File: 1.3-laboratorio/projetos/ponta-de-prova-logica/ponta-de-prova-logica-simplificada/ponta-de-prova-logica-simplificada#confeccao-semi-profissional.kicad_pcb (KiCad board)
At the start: 2 copper layers, 66 x 49.5 mm, 21 parts, among them J1 Conn_01x02, J2 PONTA DE PROVA, SW1 SW_DPDT_x2, U1 LM339

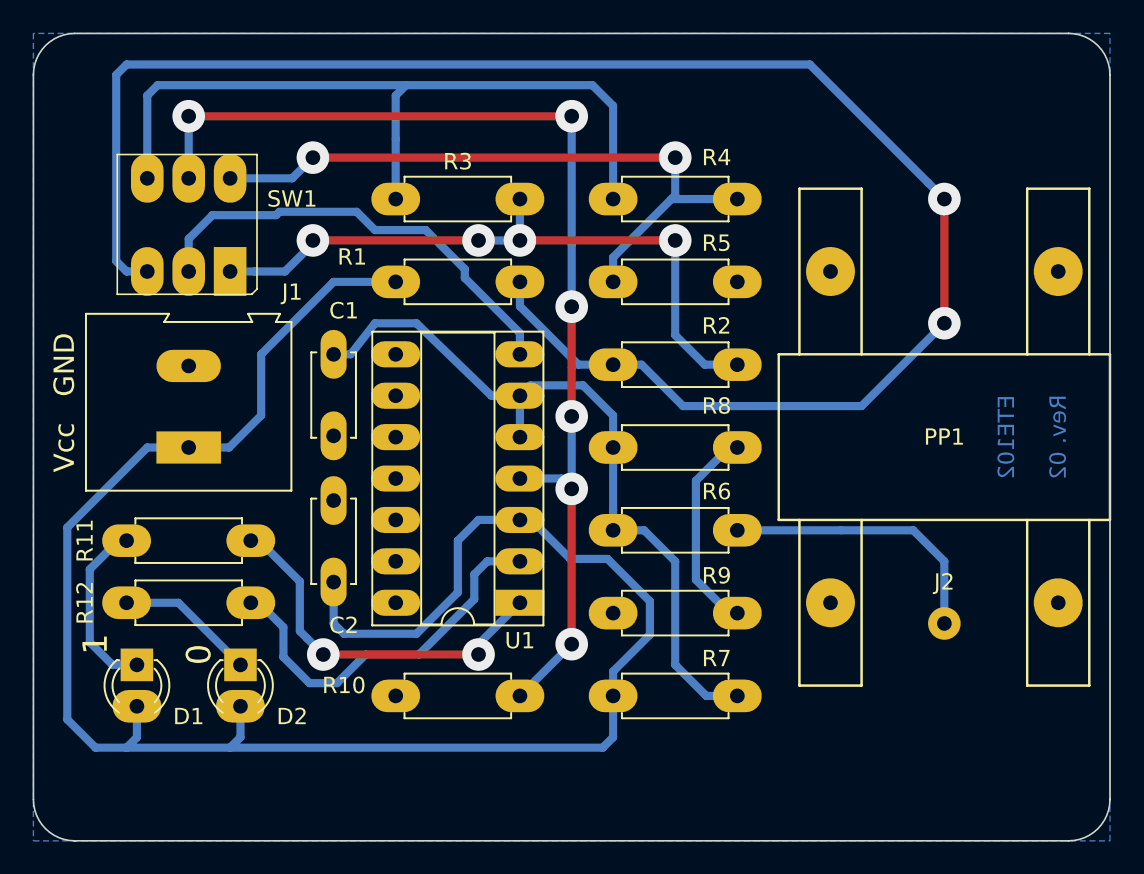
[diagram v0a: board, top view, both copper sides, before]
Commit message: Revisões no leiaute. Pontos de furação acrescentados, tamanho da placa e reposicionamento de algumas ilhas e trilhas.
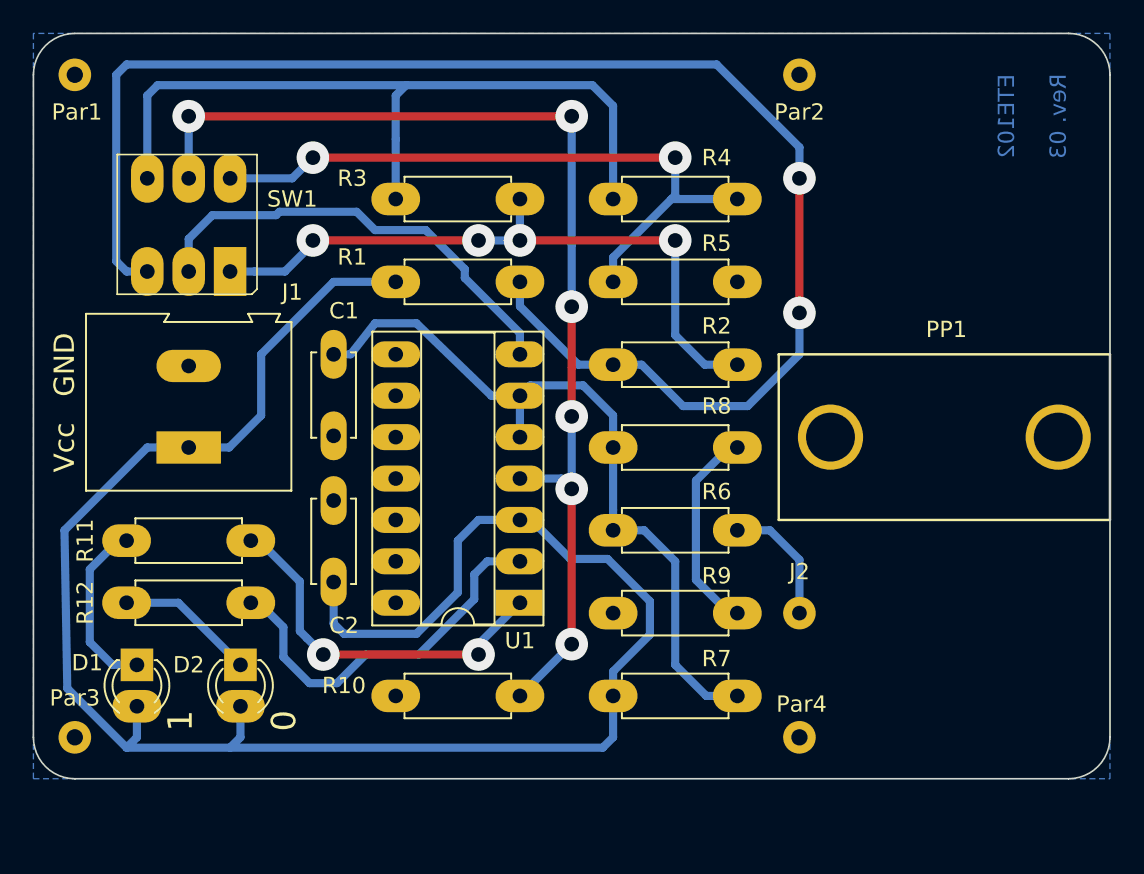
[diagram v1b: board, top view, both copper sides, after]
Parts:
- added Par1: MountingHole_1mm_M1_DIN965_Pad, MountingHole:MountingHole_2.2mm_M2_DIN965_Pad, F.Cu at (20.3, 21.0)
- added Par2: MountingHole_1mm_M1_DIN965_Pad, MountingHole:MountingHole_2.2mm_M2_DIN965_Pad, F.Cu at (64.8, 21.0)
- added Par3: MountingHole_1mm_M1_DIN965_Pad, MountingHole:MountingHole_2.2mm_M2_DIN965_Pad, F.Cu at (20.3, 61.6)
- added Par4: MountingHole_1mm_M1_DIN965_Pad, MountingHole:MountingHole_2.2mm_M2_DIN965_Pad, F.Cu at (64.8, 61.6)
- moved J2 8.91 mm to (64.8, 54.0)
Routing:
- net Net-(R1-Pad2): track 107.9 -> 93.1 mm
- net Net-(J2-Pad1): track 17.3 -> 7.83 mm
- net VCC: track 118.7 -> 117.7 mm
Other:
- board size 66 x 49.5 mm -> 66 x 45.7 mm
- board text added: "Rev. 03"
- board text removed: "Rev. 02"

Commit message: Complementações no leiaute da PCI.
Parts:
- D1: value ALTO -> VD
- D2: value BAIXO -> VM
- J2: value PONTA DE PROVA -> TP1
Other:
- board text added: "5V-15V"
- board text added: "CMOS"
- board text added: "TTL"
